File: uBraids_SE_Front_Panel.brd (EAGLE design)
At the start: 40.3 x 128.5 mm, 2 parts

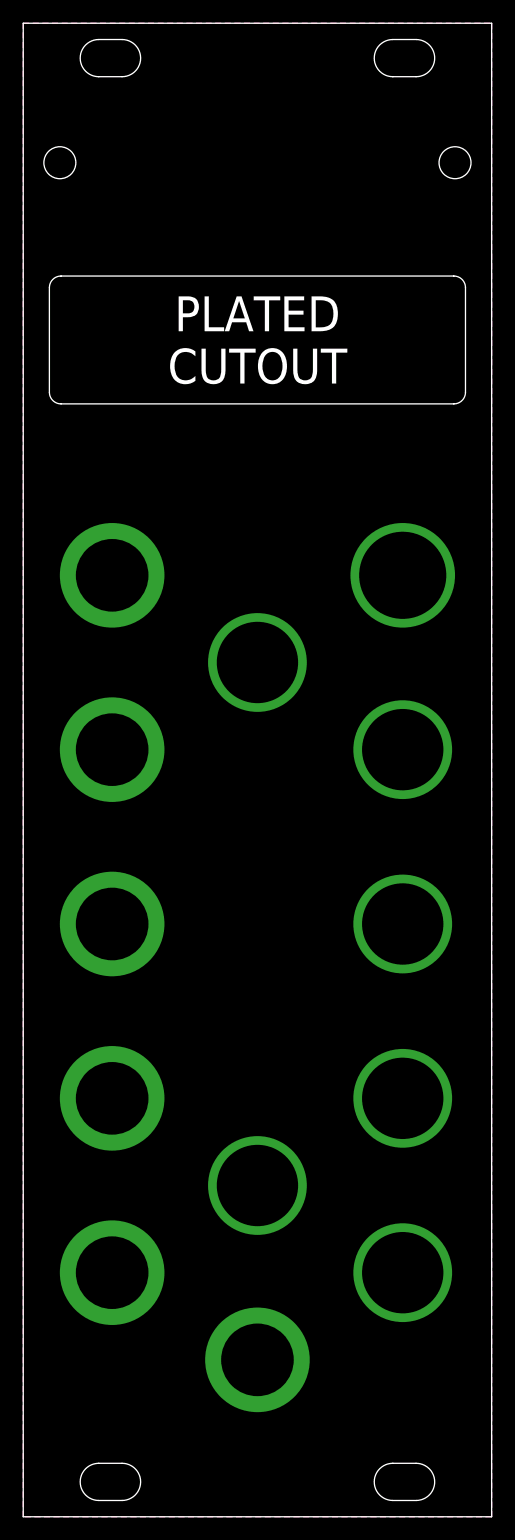
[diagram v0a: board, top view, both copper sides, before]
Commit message: update for Revision E production
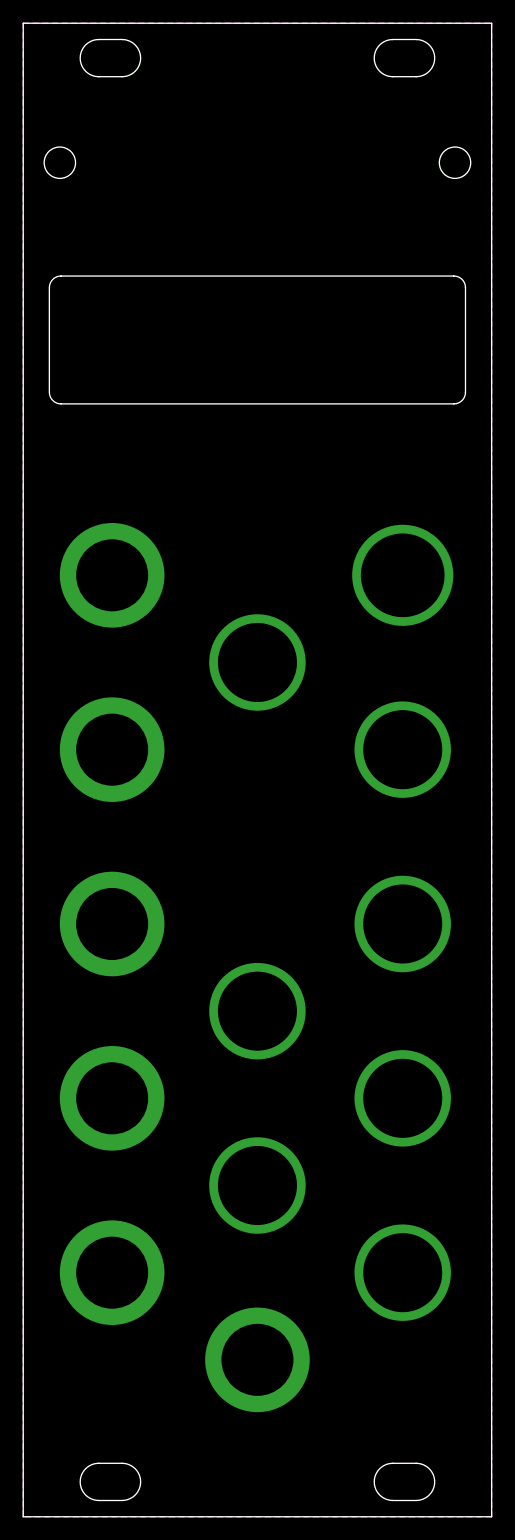
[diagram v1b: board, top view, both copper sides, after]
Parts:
- removed E$2: (no value), uBraids_SE:OSH-LOGO-5MM
- removed E$3: (no value), uBraids_SE:MARKING-CC-LOGO
- added E$7: (no value), uBraids_SE_Library:NEG-OUT
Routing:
- added copper zone on layer 1, net GND2
- added copper zone on layer 16, net GND2
- removed copper zone on layer 1, net GND
- removed copper zone on layer 16, net GND
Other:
- board text added: "11.0 MM"
- board text added: "13.0 MM"
- board text added: "35.8 MM"
- board text added: "37.8 MM"
- board text added: "COUNTERBORE TO DEPTH OF 1.0 MM ON BOTTOM SIDE (NOT PLATED)"
- board text added: "COUNTERSINK ON TOP SIDE (NOT PLATED)"
- board text added: "CUTOUT (PLATED)"
- board text added: "DO NOT PLACE ANY ADDITIONAL MARKINGS OR TEXT ON THE TOP SIDE OF THIS BOARD"
- board text added: "EDIT"
- board text added: "Panel derived from work by Olivier Gillet of Mutable Instruments, Magpie Modular, and Neutron Sound"
- board text added: "R 1.0 MM"
- board text added: "R 2.0 MM"
- board text added: "TD-UBSE-E"
- board text added: "V/OCT"
- board text added: "µBraids SE Front Panel TD-UBSE-E-FP CC BY-SA 4.0 2018-04-28 tall-dog.com"
- board text added: "⌀2.7 MM"
- board text added: "⌀5.0 MM × 90°"
- board text removed: "1V/OCT"
- board text removed: "BY-SA 4.0"
- board text removed: "OUT"
- board text removed: "PLATED CUTOUT"
- board text removed: "Panel derived from work by: Olivier Gillet of Mutable Instruments, Magpie Modular, and Neutron Sound"
- board text removed: "TALL-DOG.COM 2017-12-30 TD-UBSE-C"
- board text removed: "TD-UBSE-C"
- board text removed: "open source hardware"

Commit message: Revision F
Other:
- board text added: "TD-UBSE-F"
- board text added: "µBraids SE Front Panel TD-UBSE-F-FP/B CC BY-SA 4.0 2020-02-22 tall-dog.com"
- board text removed: "Panel derived from work by Olivier Gillet of Mutable Instruments, Magpie Modular, and Neutron Sound"
- board text removed: "TD-UBSE-E"
- board text removed: "µBraids SE Front Panel TD-UBSE-E-FP CC BY-SA 4.0 2018-04-28 tall-dog.com"
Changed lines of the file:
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@@
 <?xml version="1.0" encoding="utf-8"?>
 <!DOCTYPE eagle SYSTEM "eagle.dtd">
-<eagle version="9.0.0">
+<eagle version="9.5.2">
 <drawing>
 <settings>
@@
 <setting verticaltext="up"/>
 </settings>
-<grid distance="0.1" unitdist="mm" unit="mm" style="lines" multiple="1" display="yes" altdistance="0.025" altunitdist="inch" altunit="inch"/>
+<grid distance="0.5" unitdist="mm" unit="mm" style="lines" multiple="1" display="yes" altdistance="0.025" altunitdist="inch" altunit="inch"/>
 <layers>
 <layer number="1" name="Top" color="4" fill="1" visible="yes" active="yes"/>
@@
 <wire x1="31.8" y1="127.1" x2="33.8" y2="127.1" width="0" layer="20"/>
 <wire x1="31.8" y1="123.9" x2="33.8" y2="123.9" width="0" layer="20"/>
-<text x="20.15" y="58.5" size="1.5" layer="30" ratio="10" rot="MR0" align="center">Panel derived
-from work by
-Olivier Gillet of
-Mutable Instruments,
-Magpie Modular,
-and Neutron
-Sound</text>
 <text x="20.15" y="120" size="1.5" layer="29" ratio="10" align="center">tall-dog.com</text>
-<text x="20.15" y="125.5" size="1.5" layer="29" ratio="10" align="center">TD-UBSE-E</text>
+<text x="20.15" y="125.5" size="1.5" layer="29" ratio="10" align="center">TD-UBSE-F</text>
 <wire x1="13.4" y1="127" x2="26.9" y2="127" width="0.15" layer="29"/>
 <wire x1="26.9" y1="127" x2="26.9" y2="124" width="0.15" layer="29"/>
@@
 <wire x1="7.65" y1="21" x2="20.15" y2="28.5" width="0.25" layer="29"/>
 <wire x1="32.65" y1="21" x2="20.15" y2="28.5" width="0.25" layer="29"/>
-<text x="20.15" y="127" size="1.5" layer="30" ratio="10" rot="MR0" align="top-center">µBraids SE
+<text x="20.15" y="126.5" size="2" layer="30" ratio="12" rot="MR0" align="top-center">µBraids SE
 Front Panel
-TD-UBSE-E-FP
+TD-UBSE-F-FP/B
 CC BY-SA 4.0
-2018-04-28
+2020-02-22
 tall-dog.com</text>
 <circle x="16.65" y="4.5" radius="1" width="0" layer="29"/>
@@
 <param name="checkStop" value="0"/>
 <param name="checkValues" value="0"/>
+<param name="checkNames" value="1"/>
+<param name="checkWireStubs" value="1"/>
+<param name="checkPolygonWidth" value="0"/>
 <param name="useDiameter" value="13"/>
 <param name="maxErrors" value="50"/>
@@
 </autorouter>
 <elements>
-<element name="E$7" library="uBraids_SE_Library" package="NEG-OUT" value="" x="20.15" y="6"/>
+<element name="E$7" library="uBraids_SE_Library" package="NEG-OUT" value="" x="20.15" y="6" smashed="yes"/>
 </elements>
 <signals>
@@
 </signal>
 </signals>
+<mfgpreviewcolors>
+<mfgpreviewcolor name="soldermaskcolor" color="0xC8008000"/>
+<mfgpreviewcolor name="silkscreencolor" color="0xFFFEFEFE"/>
+<mfgpreviewcolor name="backgroundcolor" color="0xFF282828"/>
+<mfgpreviewcolor name="coppercolor" color="0xFFFFBF00"/>
+<mfgpreviewcolor name="substratecolor" color="0xFF786E46"/>
+</mfgpreviewcolors>
 <errors>
 </errors>
